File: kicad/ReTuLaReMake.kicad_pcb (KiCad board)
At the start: 2 copper layers, 54 x 26 mm, 28 parts, among them J1 40 Pin DIP Header, J2 Conn_02x05_Odd_Even, J3 Conn_01x01_Male, U1 ATF1508AS-10AU100

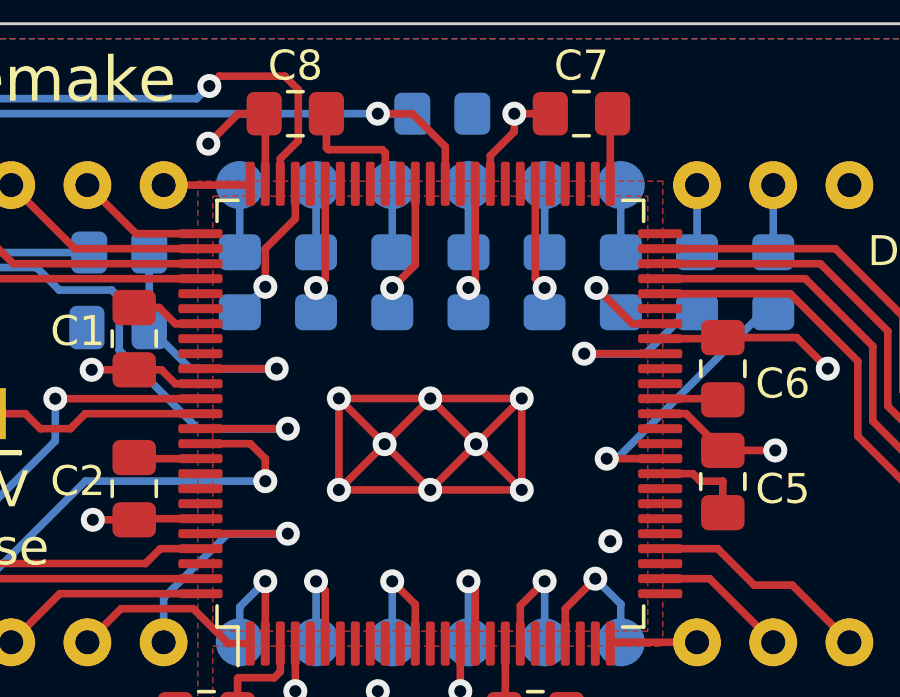
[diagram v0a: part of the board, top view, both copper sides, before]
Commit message: KiCAD: Move vias off pads
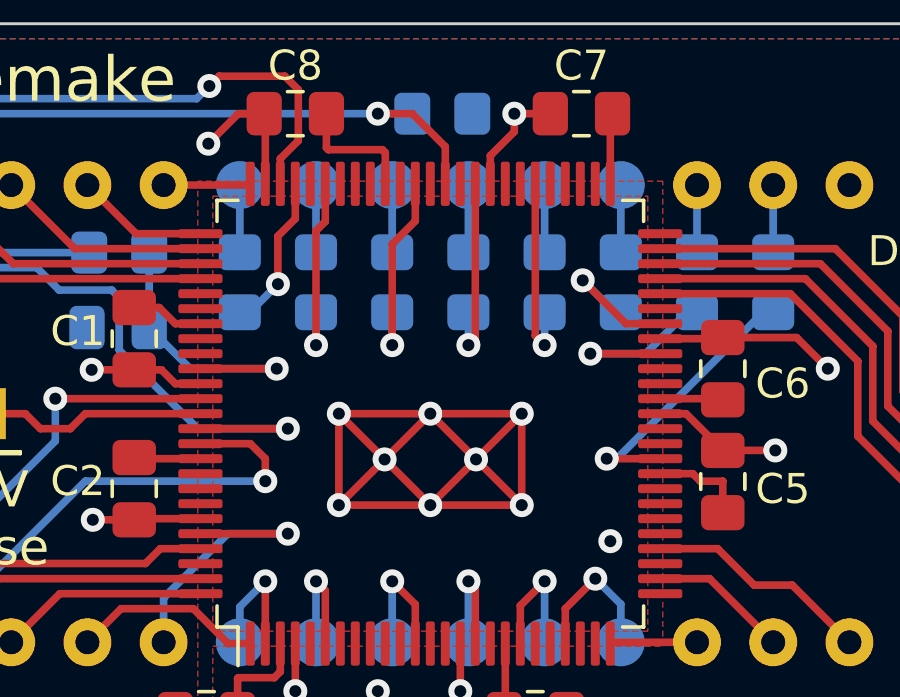
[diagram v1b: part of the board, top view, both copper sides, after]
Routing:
- net /HD5: track 4.60 -> 6.79 mm
- net /HD4: track 4.38 -> 6.57 mm
- net /HD3: track 4.41 -> 6.60 mm
- net /HD6: track 4.41 -> 6.60 mm
- net /HD2: track 3.76 -> 4.69 mm

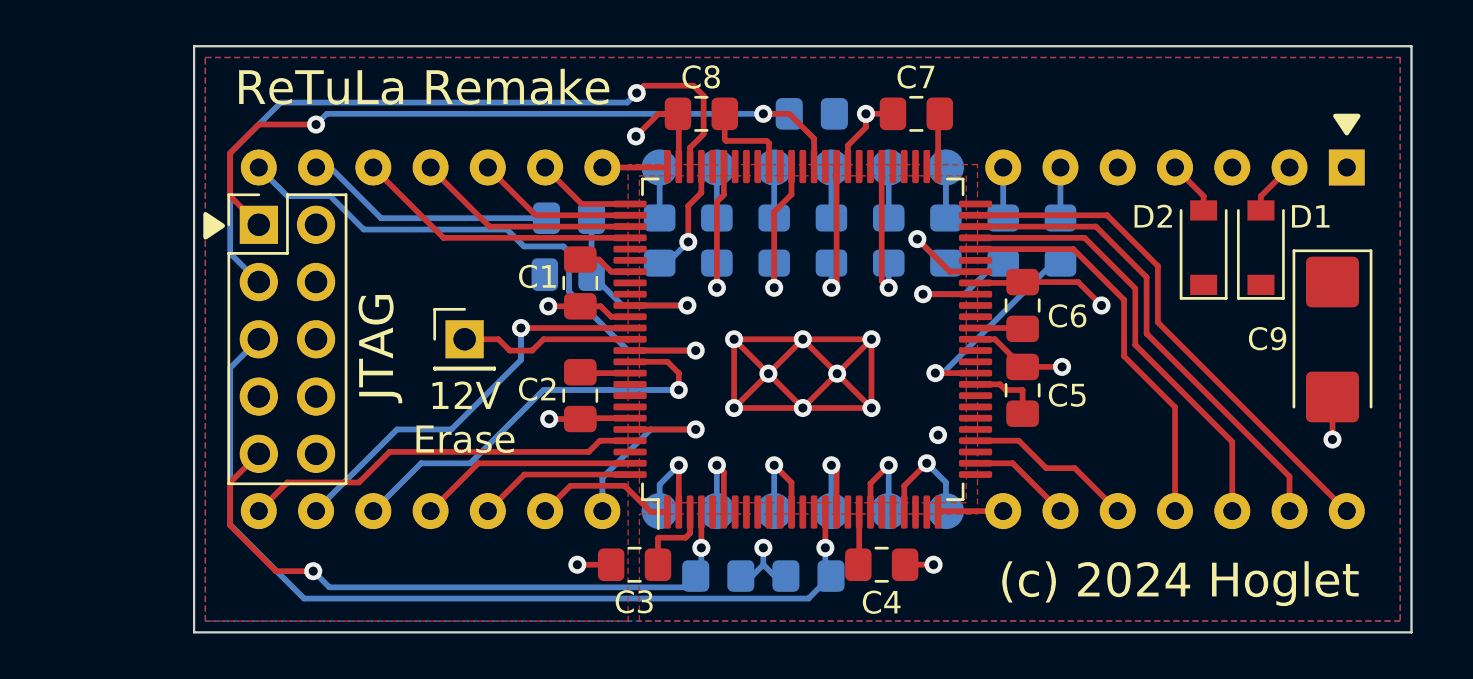
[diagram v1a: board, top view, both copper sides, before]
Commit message: KiCAD: Rotate board so text the right way up
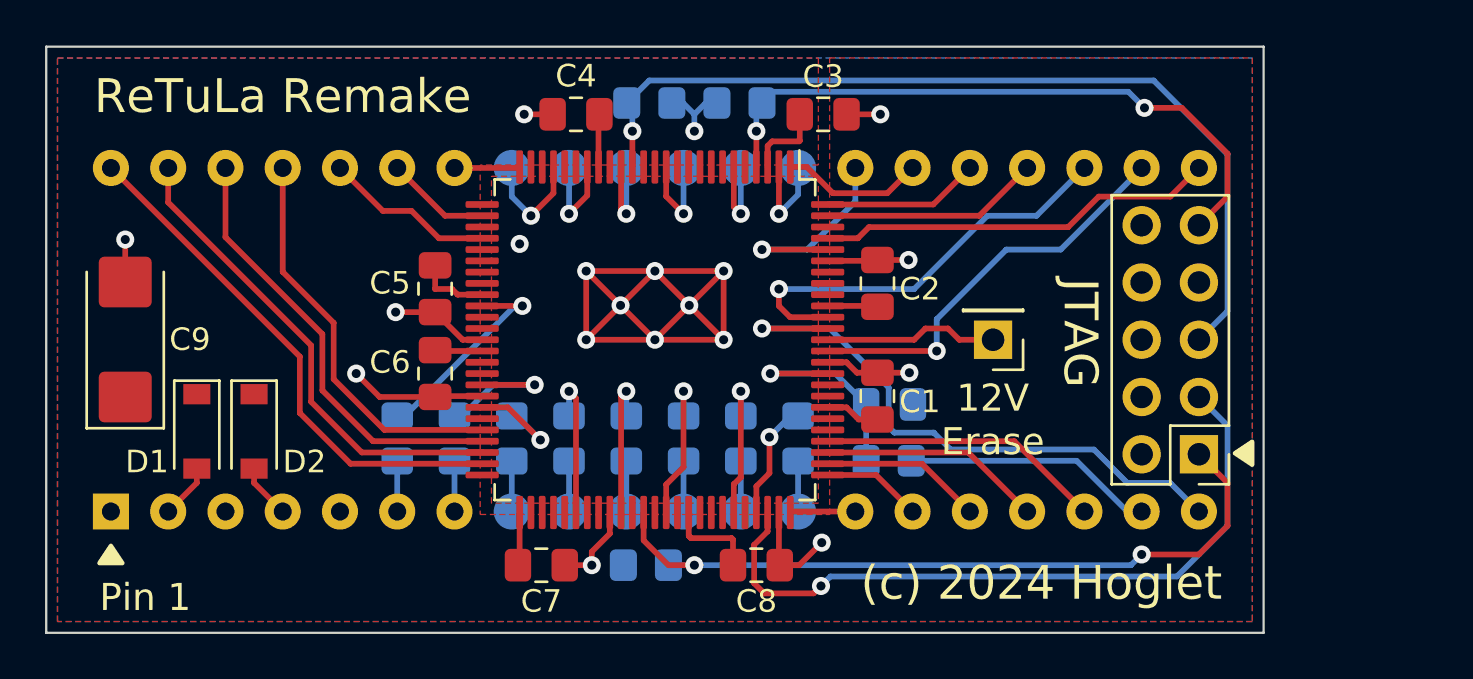
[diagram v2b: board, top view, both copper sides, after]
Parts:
- moved J1 56.9 mm to (96.3, 127.0), turned to -90 degrees
- moved C9 53.6 mm to (96.9, 119.4), turned to 90 degrees
- moved D1 47.9 mm to (100.1, 123.5), turned to -90 degrees
- moved J2 42.9 mm to (144.6, 124.5), turned to 180 degrees
- moved D2 42.9 mm to (102.7, 123.5), turned to -90 degrees
- moved R1 30.7 mm to (109.0, 123.8), turned to -90 degrees
- moved C5 26.4 mm to (110.7, 117.1), turned to -90 degrees
- moved C6 26.2 mm to (110.7, 120.9), turned to -90 degrees
- moved C7 26.0 mm to (115.4, 129.4), turned to 0 degrees
- moved R2 25.9 mm to (111.5, 123.8), turned to -90 degrees
- moved C4 24.1 mm to (116.9, 109.4), turned to 180 degrees
- moved J3 23.4 mm to (135.4, 119.4), turned to 180 degrees
- moved R11 22.1 mm to (120.2, 108.9), turned to 0 degrees
- moved C3 21.7 mm to (127.9, 109.4), turned to 0 degrees
- moved R12 21.3 mm to (120.0, 129.4), turned to 180 degrees
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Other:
- board text added: "Pin 1"

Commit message: KiCAD: Remove R1-R8
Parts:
- removed the R1 at (109.0, 123.8)
- removed the R2 at (111.5, 123.8)
- removed the R3 at (114.1, 123.8)
- removed the R4 at (116.6, 123.8)
- removed R5, R6, R7, R8: 0R, Resistor_SMD:R_0805_2012Metric_Pad1.20x1.40mm_HandSolder
- renumbered R9 to R1, R10 to R2, R11 to R3, R12 to R4
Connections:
- J1 pad 10: Net-(J1-Pad10) -> /HD4
- J1 pad 11: Net-(J1-Pad11) -> /HD5
- J1 pad 12: Net-(J1-Pad12) -> /HD6
- J1 pad 13: Net-(J1-Pad13) -> /HD7
- J1 pad 6: Net-(J1-Pad6) -> /HD0
- J1 pad 7: Net-(J1-Pad7) -> /HD1
- J1 pad 8: Net-(J1-Pad8) -> /HD2
- J1 pad 9: Net-(J1-Pad9) -> /HD3
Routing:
- net /HD0: track 9.02 -> 13.4 mm
- net /HD1: track 6.12 -> 9.43 mm
- net Net-(J1-Pad9): track 2.24 -> 0.00 mm
- net Net-(J1-Pad8): track 2.24 -> 0.00 mm
- net Net-(J1-Pad7): track 2.24 -> 0.00 mm
- net Net-(J1-Pad6): track 2.24 -> 0.00 mm
- net Net-(J1-Pad13): track 2.24 -> 0.00 mm
- net Net-(J1-Pad12): track 2.24 -> 0.00 mm
- net Net-(J1-Pad11): track 2.24 -> 0.00 mm
- net Net-(J1-Pad10): track 2.24 -> 0.00 mm
- net /HD2: track 4.69 -> 6.23 mm
- net /HD4: track 6.57 -> 5.22 mm
- net /HD3: track 6.60 -> 5.25 mm
- net /HD6: track 6.60 -> 5.25 mm
- net /HD5: track 6.79 -> 5.44 mm
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
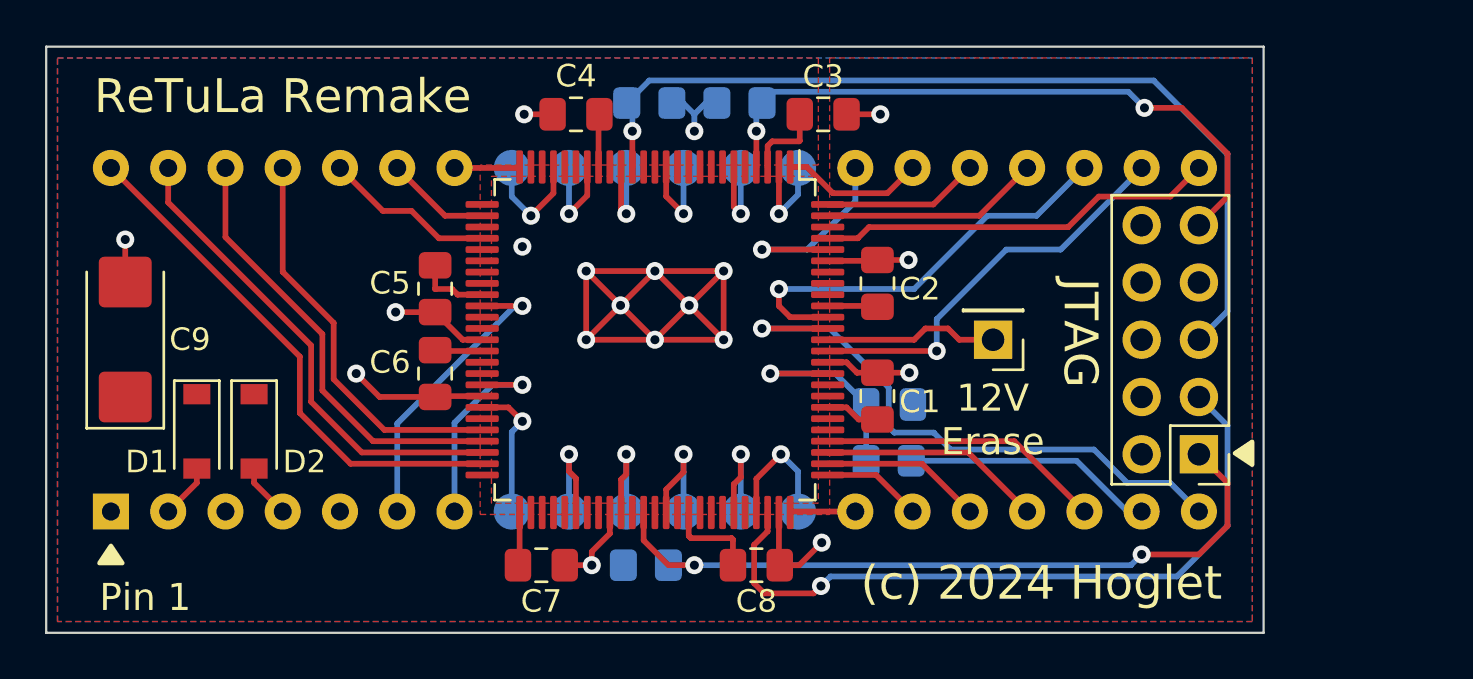
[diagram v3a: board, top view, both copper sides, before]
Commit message: KiCAD: Reduce via size to 0.7/0.3mm, add more GND vias
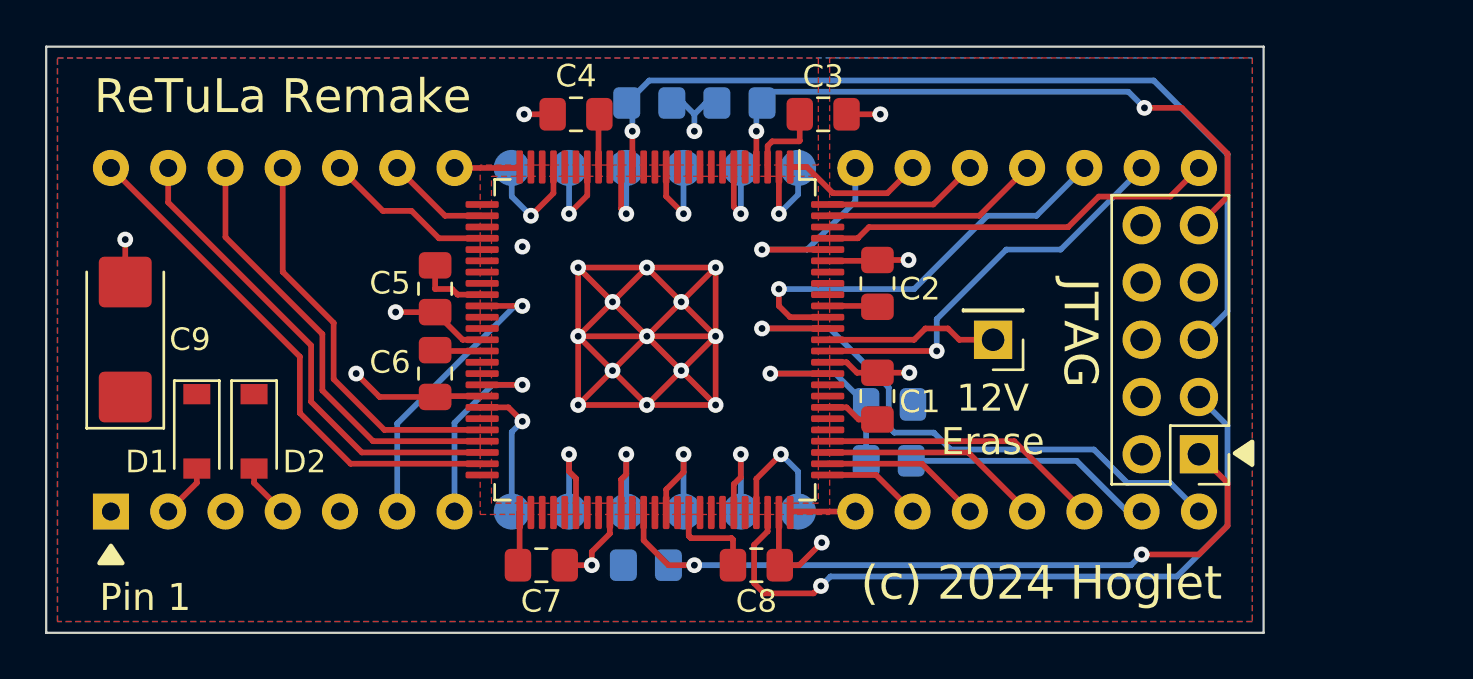
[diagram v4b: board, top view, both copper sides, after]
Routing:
- net GND: track 66.3 -> 95.7 mm, vias 18 -> 23

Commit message: KiCAD: Move clock filter to top side
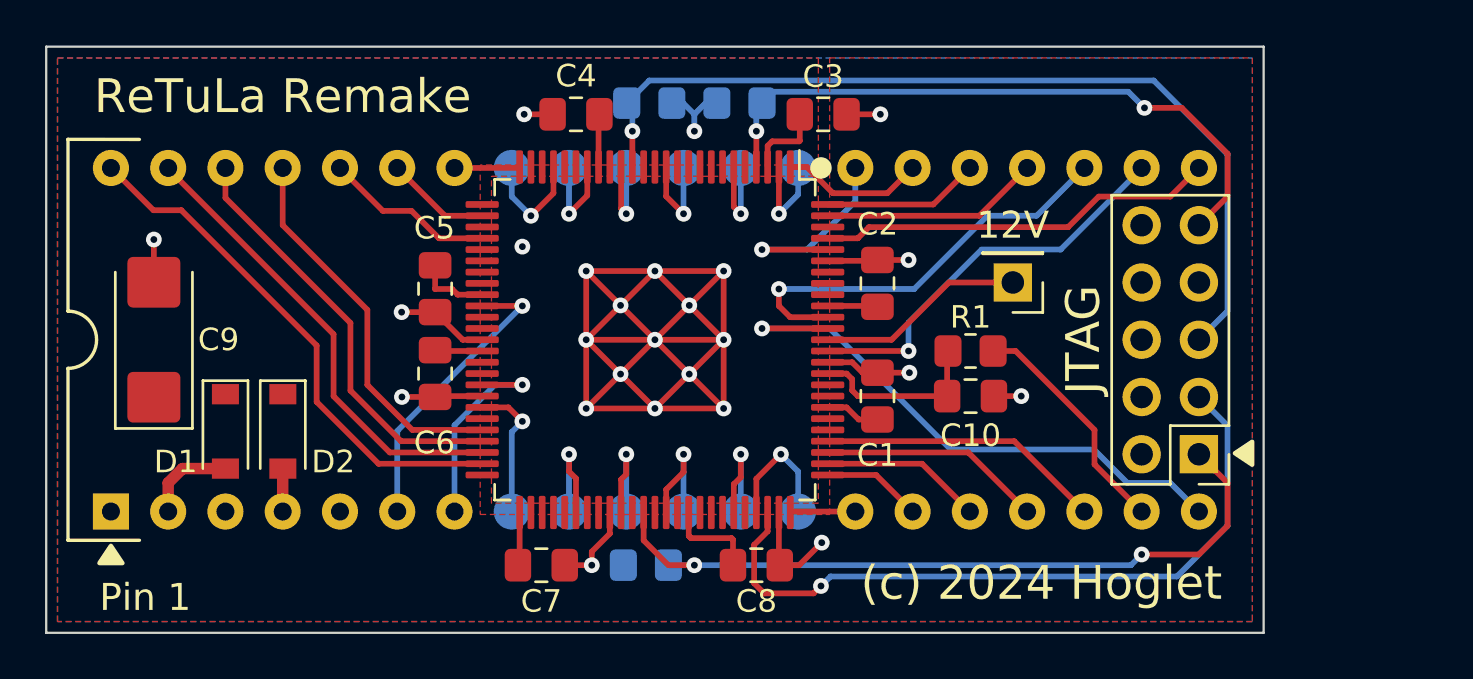
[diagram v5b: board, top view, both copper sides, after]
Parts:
- C10, R1: moved to F.Cu
- moved R1 6.07 mm to (134.4, 119.9)
- moved C10 3.61 mm to (134.4, 121.9)
- moved J3 2.69 mm to (136.3, 116.9)
- moved D2 1.28 mm to (103.9, 123.5)
- moved C9 1.27 mm to (98.2, 119.4)
- moved D1 1.27 mm to (101.4, 123.5)
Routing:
- net /HO2filtered: track 9.86 -> 7.97 mm, vias 1 -> 0
- net Net-(D1-Pad2): track 2.43 -> 4.07 mm
- net Net-(J3-Pad1): track 7.75 -> 9.26 mm
- net GND: track 95.7 -> 94.2 mm, vias 23 -> 24
- net /HRST: track 26.7 -> 25.7 mm
- net /HIRQ: track 21.5 -> 20.7 mm
- net /PRST: track 17.8 -> 17.1 mm
- net /DRQ: track 19.7 -> 18.9 mm
- net Net-(D2-Pad2): track 2.43 -> 1.90 mm
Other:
- board text added: "12V"
- board text removed: "12V Erase"

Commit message: KiCAD: Move R2/3/4 to top side
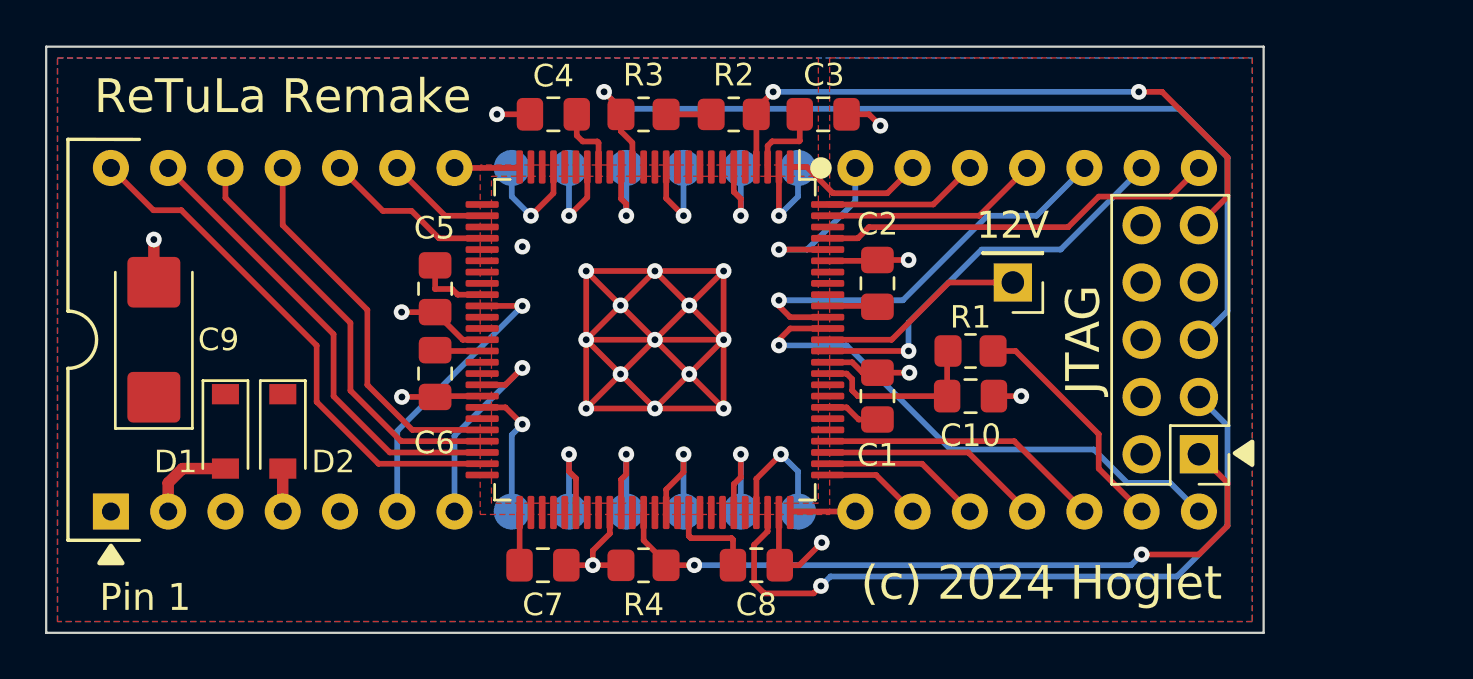
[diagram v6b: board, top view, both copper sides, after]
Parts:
- R2, R3, R4: moved to F.Cu
- moved C4 1.00 mm to (115.9, 109.4)
- moved R2 0.57 mm to (123.9, 109.4)
- moved R3 0.57 mm to (119.9, 109.4)
- moved R4 0.11 mm to (119.9, 129.4)
- moved C7 0.07 mm to (115.5, 129.4)
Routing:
- net GND: track 94.2 -> 95.9 mm
- net /PA0: track 9.42 -> 7.92 mm
- net /HRST: track 25.7 -> 24.3 mm
- net /TMS: track 39.8 -> 41.1 mm
- net /TCK: track 33.2 -> 32.0 mm
- net VCC: track 25.5 -> 25.2 mm, vias 1 -> 0
